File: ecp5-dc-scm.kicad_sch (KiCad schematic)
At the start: 2 parts

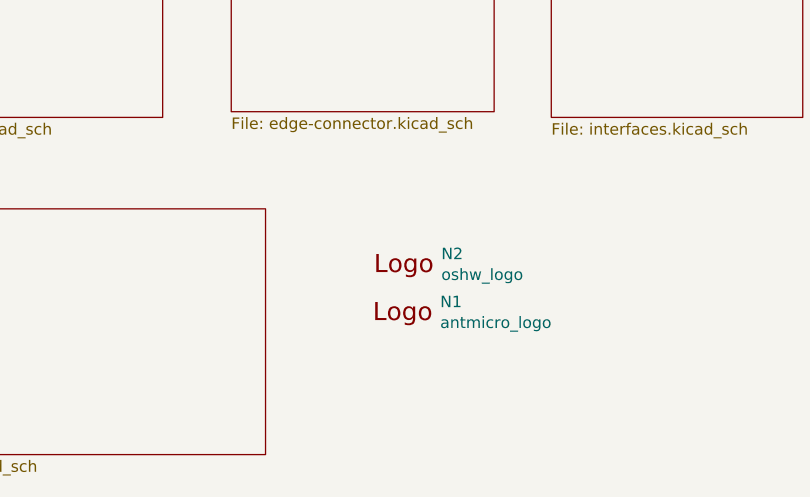
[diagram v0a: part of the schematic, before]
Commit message: [#61392] Convert project to KiCad 7
[#61392] Run globlib

[#61392] Allign components to the grid

[#61392] Update oshw and antmicro logo

[#61392] Standarize ethernet sheet

[#61392] Standarize pcie-conn sheet

[#61392] Standarize rot sheet

[#61392] Standarize edge-connector sheet

[#61392] WIP:Standarize interfaces sheet

[#61392] WIP: Route interfaces sheet

[#61392] Finish standarizing interfaces sheet

[#61392] Update interfaces sheet with fixed 2N7002

[#61392] WIP:Standarize ddr3 sheet

[#61392] Standarize ddr3 sheet

[#61392] Standarize power-supply sheet

[#61392] Standarize fpga power-supply sheet

[#61392] Remove TODO comments from power-banks sheet

[#61392] Standarize fpga-banks sheet

[#61392] Ignore Input pins not driven ERC

[#61392] Clear off grid ERCs

[#61392] Exclude ERC DDR3_VTT_EN NC

[#61392] Bump rev to 1.2.1

[#61392] Bump PCB rev to 1.2.1
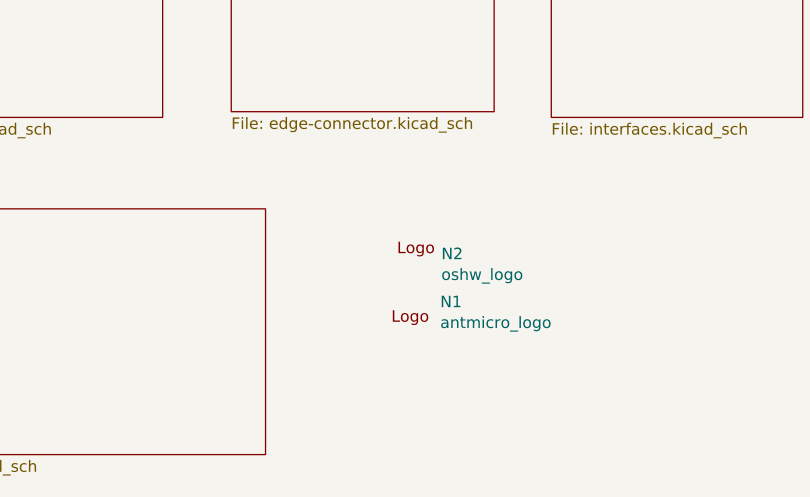
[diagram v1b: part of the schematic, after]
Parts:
- N1: footprint ecp5-dc-scm-footprints:antmicro-logo_scaled_20mm -> antmicro-footprints:antmicro-logo; symbol ecp5-dc-scm:antmicro_logo -> antmicroMechanicalParts:antmicro_logo; Author (none) -> Antmicro; License (none) -> Apache-2.0; Public (none) -> False
- N2: footprint ecp5-dc-scm-footprints:oshw-logo -> antmicro-footprints:oshw-logo; symbol ecp5-dc-scm:oshw_logo -> antmicroMechanicalParts:oshw_logo; Author (none) -> Antmicro; License (none) -> Apache-2.0; Public (none) -> False
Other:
- moved on the sheet: N1, N2

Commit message: [#61392] Import changes to the PCB
[#61392] Fix D2 orientation

[#61392] Fix J2 J1 D6 orientation

[#61392] WIP: PCB Fix caps orienations

[#61392] PCB Fix caps orienations

[#61392] Fix missalligned edge cuts

[#61392] Sync Sch with PCB

[#61392] Fix silk clipped by edge cuts

[#61392] Ignore TP no courtyard drc

[#61392] Update C_0603 footprints

[#61392] Update R_0402 footprints

[#61392] Update Sot-23 footprints

[#61392] Update QFN and IHLP footprints

[#61392] Update remaining footprints

[#61392] Change minimal text height to 0.7mm

[#61392] Clear remaining Silk DRCs

[#61392] Update TPS51200DRCT symbol

[#61392] Update 9774040151

[#61392] Update W25Q32JVS

[#61392] Update ECS-3225MVQ-1000CN-TR

[#61392] Clean ERC

[#61392] Remove obsolete files

[#61392] Synhronize components with library

[#61392] Remove globlib leftovers

[#61392] Synchronize components with libraries (WiP)

[#61392] Clean ERC and DRC

[#61392] Set J5 to DNP

[#61392] Add PCB SHA string, update layer names

[#61392] Update assets

[#62567] Add stackup.csv

[#62567] Input elecric constants for the board stackup

[#62567] Update stackup.csv
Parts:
- N1: footprint antmicro-footprints:antmicro-logo -> antmicro-footprints:antmicro-logo_scaled_20mm
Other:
- moved on the sheet: N1
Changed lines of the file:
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@@
   (title_block
     (title "ECP5 - Datacenter Secure Control Module (DC-SCM)")
-    (date "2024-07-01")
+    (date "2024-07-15")
     (rev "1.2.1")
   )
@@
   (symbol (lib_id "antmicroMechanicalParts:oshw_logo") (at 148.59 170.18 0) (unit 1)
     (in_bom yes) (on_board yes) (dnp no)
-    (property "Reference" "N2" (at 153.5176 170.1038 0)
+    (property "Reference" "N2" (at 153.67 168.91 0)
       (effects (font (size 1.27 1.27)) (justify left))
     )
-    (property "Value" "oshw_logo" (at 153.5176 172.4152 0)
+    (property "Value" "oshw_logo" (at 153.67 171.2214 0)
       (effects (font (size 1.27 1.27)) (justify left))
     )
@@
     )
   )
-  (symbol (lib_id "antmicroMechanicalParts:antmicro_logo") (at 147.955 177.8 0) (unit 1)
+  (symbol (lib_id "antmicroMechanicalParts:antmicro_logo") (at 148.59 177.8 0) (unit 1)
     (in_bom yes) (on_board yes) (dnp no)
-    (property "Reference" "N1" (at 153.3906 175.4378 0)
+    (property "Reference" "N1" (at 154.0256 175.4378 0)
       (effects (font (size 1.27 1.27)) (justify left))
     )
-    (property "Value" "antmicro_logo" (at 153.3906 177.7492 0)
+    (property "Value" "antmicro_logo" (at 154.0256 177.7492 0)
       (effects (font (size 1.27 1.27)) (justify left))
     )
-    (property "Footprint" "antmicro-footprints:antmicro-logo" (at 145.415 171.45 0)
+    (property "Footprint" "antmicro-footprints:antmicro-logo_scaled_20mm" (at 146.05 171.45 0)
       (effects (font (size 1.27 1.27)) hide)
     )
-    (property "Datasheet" "" (at 147.955 168.91 0)
+    (property "Datasheet" "" (at 148.59 168.91 0)
       (effects (font (size 1.27 1.27)) hide)
     )
-    (property "MPN" "" (at 147.955 177.8 0)
+    (property "MPN" "" (at 148.59 177.8 0)
       (effects (font (size 1.27 1.27)))
     )
-    (property "Manufacturer" "" (at 163.195 198.12 0)
+    (property "Manufacturer" "" (at 163.83 198.12 0)
       (effects (font (size 1.27 1.27) (thickness 0.15)) (justify left bottom) hide)
     )
-    (property "Author" "Antmicro" (at 163.195 193.04 0)
+    (property "Author" "Antmicro" (at 163.83 193.04 0)
       (effects (font (size 1.27 1.27) (thickness 0.15)) (justify left bottom) hide)
     )
-    (property "License" "Apache-2.0" (at 163.195 195.58 0)
+    (property "License" "Apache-2.0" (at 163.83 195.58 0)
       (effects (font (size 1.27 1.27) (thickness 0.15)) (justify left bottom) hide)
     )
-    (property "Public" "False" (at 163.195 198.12 0)
+    (property "Public" "False" (at 163.83 198.12 0)
       (effects (font (size 1.27 1.27)) (justify left bottom) hide)
     )
